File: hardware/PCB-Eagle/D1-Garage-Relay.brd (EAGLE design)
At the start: 72.1 x 39.4 mm, 20 parts, among them J1 BME680, J2 Door1, J3 Door2, J4 Door2-IN, J5 Door1-IN

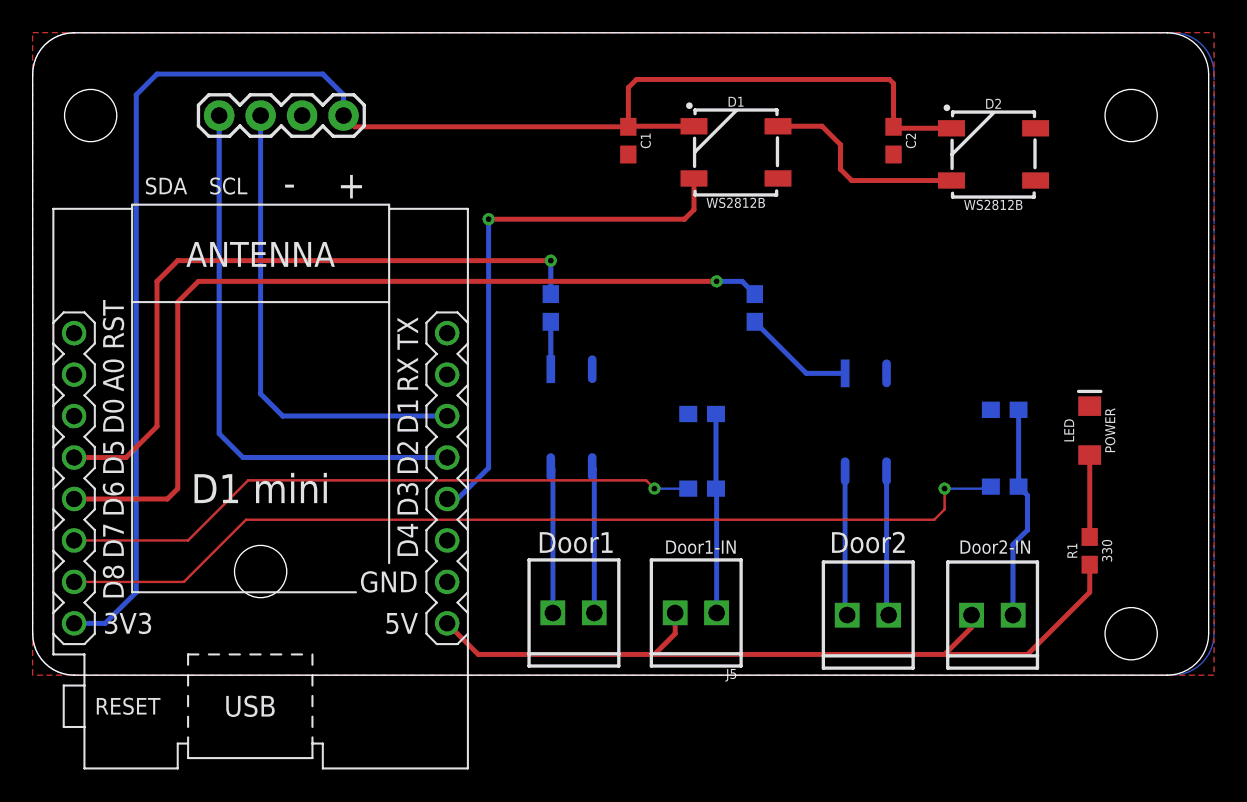
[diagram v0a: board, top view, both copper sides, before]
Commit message: adjusted bottom layer to accomodate documentation
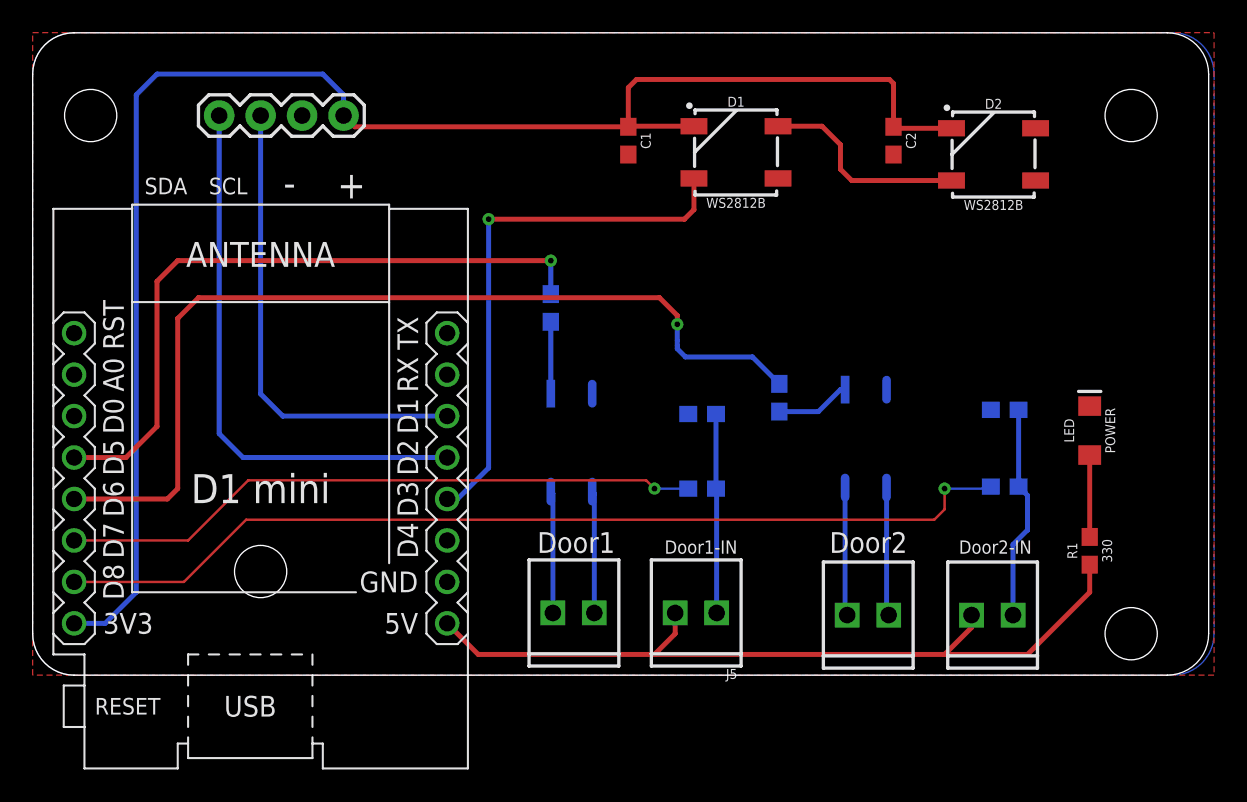
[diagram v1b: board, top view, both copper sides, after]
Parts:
- moved R7 5.70 mm to (45.8, 17.0)
- moved RELAY1 1.50 mm to (33.0, 14.2)
- moved RELAY2 1.00 mm to (51.1, 14.5)
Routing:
- net DOOR2: track 54.3 -> 57.8 mm
- net N$9: track 6.84 -> 4.59 mm
- net N$6: track 2.90 -> 4.40 mm
- net N$5: track 8.99 -> 7.49 mm
- net N$1: track 8.99 -> 7.49 mm
- net N$7: track 8.86 -> 7.86 mm
- net N$2: track 8.86 -> 7.86 mm
